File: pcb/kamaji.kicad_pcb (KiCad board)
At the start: 2 copper layers, 130 x 110 mm, 35 parts, among them J1 RJ10, J2 RJ10, J3 RJ10, J4 RJ10, J5 RJ10, Q1 TIP120, Q2 TIP120, SW1 CTRL1, SW2 CTRL2, SW3 CTRL3, U1 ATMEGA328P-PU

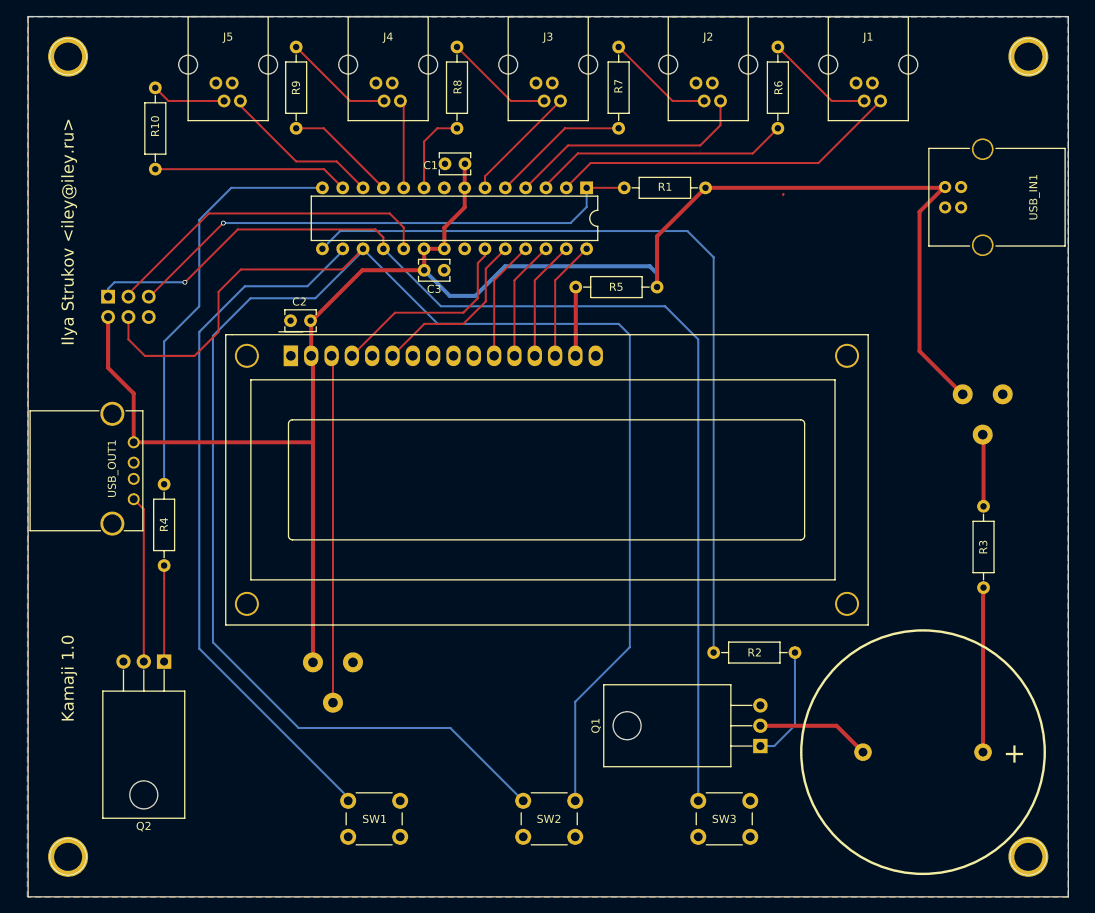
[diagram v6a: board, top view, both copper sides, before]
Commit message: replace TIP120 with a MOSFET, drive the speaker directly
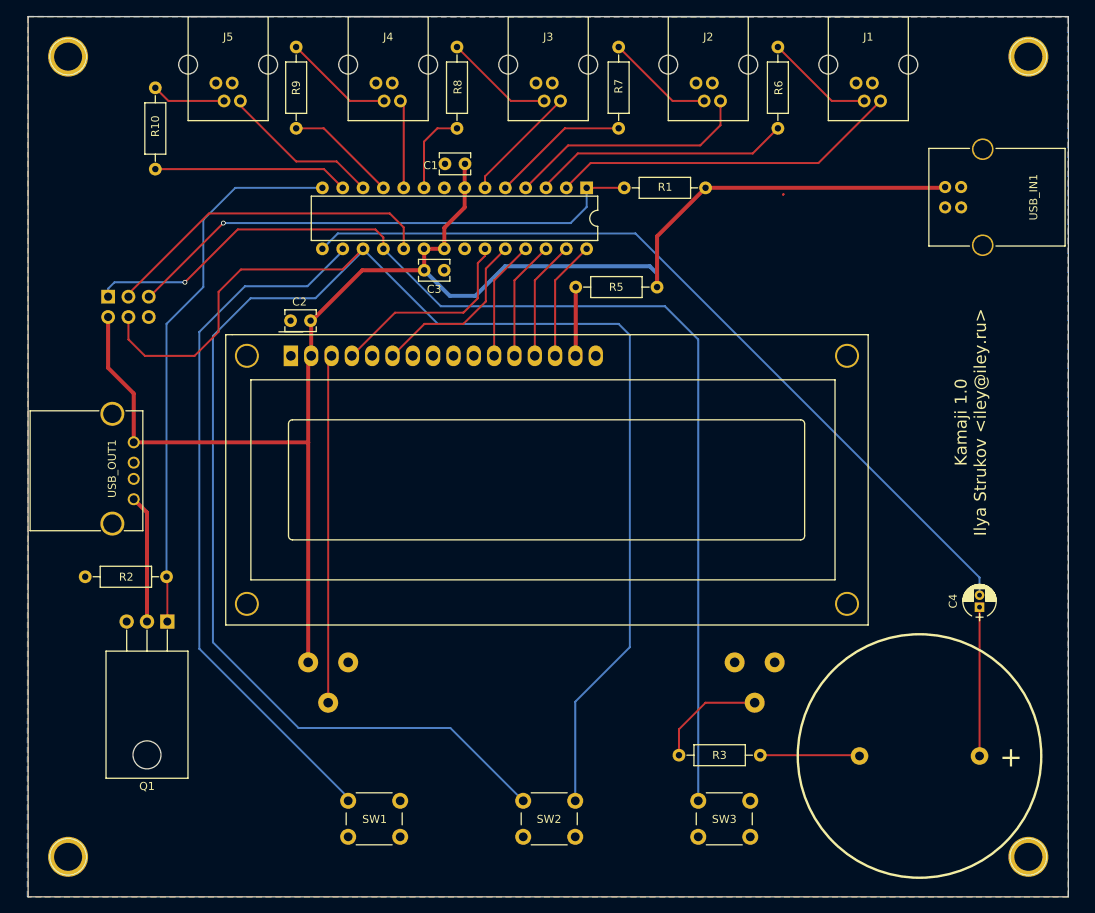
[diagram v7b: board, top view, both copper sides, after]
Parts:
- removed Q2: TIP120, TO_SOT_Packages_THT:TO-220_Horizontal
- removed R4: 2.2K, Resistors_THT:R_Axial_DIN0207_L6.3mm_D2.5mm_P10.16mm_Horizontal
- added C4: 47u, Capacitors_THT:CP_Radial_D4.0mm_P1.50mm, F.Cu at (218.9, 103.8)
- Q1: value TIP120 -> IRF540N
- R2: value 220R -> 10K
- R3: value 20R -> 100R
- moved R2 79.1 mm to (117.3, 100.0)
- moved Q1 75.7 mm to (117.4, 105.6), turned to 180 degrees
- moved RV1 44.0 mm to (188.3, 110.7)
- moved R3 41.8 mm to (191.5, 122.3), turned to 180 degrees
- moved LS1 0.65 mm to (211.4, 122.4)
- moved RV2 0.60 mm to (135.0, 110.7)
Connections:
- DS1 pad 10: Net-(DS1-Pad10) -> (no net)
- DS1 pad 7: Net-(DS1-Pad7) -> (no net)
- DS1 pad 8: Net-(DS1-Pad8) -> (no net)
- DS1 pad 9: Net-(DS1-Pad9) -> (no net)
- LS1 pad 1: Net-(LS1-Pad1) -> Net-(C4-Pad1)
- Q1 pad 1: Net-(Q1-Pad1) -> LAMP
- Q1 pad 2: Net-(LS1-Pad2) -> Net-(Q1-Pad2)
- R2 pad 1: Net-(Q1-Pad1) -> LAMP
- R2 pad 2: SND -> GND
- R3 pad 1: Net-(R3-Pad1) -> Net-(LS1-Pad2)
- R3 pad 2: Net-(LS1-Pad1) -> Net-(R3-Pad2)
- RV1 pad 1: VCC -> (no net)
- RV1 pad 2: Net-(R3-Pad1) -> Net-(R3-Pad2)
- RV1 pad 3: Net-(RV1-Pad3) -> GND
- USB_IN1 pad 2: Net-(USB_IN1-Pad2) -> (no net)
- USB_IN1 pad 3: Net-(USB_IN1-Pad3) -> (no net)
- USB_OUT1 pad 2: Net-(USB_OUT1-Pad2) -> (no net)
- USB_OUT1 pad 3: Net-(USB_OUT1-Pad3) -> (no net)
- USB_OUT1 pad 4: Net-(Q2-Pad2) -> Net-(Q1-Pad2)
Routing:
- net VCC: track 224.5 -> 195.0 mm
- net Net-(Q2-Pad2): track 20.8 -> 0.00 mm
- net Net-(LS1-Pad1): track 20.6 -> 0.00 mm
- net Net-(C4-Pad1): track 0.00 -> 18.6 mm
- net LAMP: track 51.9 -> 68.7 mm
- net Net-(Q1-Pad2): track 0.00 -> 16.0 mm
- net Net-(Q1-Pad1): track 14.5 -> 0.00 mm
- net Net-(R3-Pad2): track 0.00 -> 14.1 mm
- net Net-(Q2-Pad1): track 12.0 -> 0.00 mm
- net Net-(R3-Pad1): track 9.14 -> 0.00 mm
- net SND: track 100.6 -> 102.9 mm
- net Net-(LS1-Pad2): track 14.2 -> 12.6 mm
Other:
- board text added: "Kamaji 1.0 Ilya Strukov <iley@iley.ru>"
- board text removed: "Ilya Strukov <iley@iley.ru>"
- board text removed: "Kamaji 1.0"

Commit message: fix mounting holes
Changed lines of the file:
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@@
     (mod_text_width 0.15)
     (pad_size 5 5)
-    (pad_drill 3.5)
+    (pad_drill 3.3)
     (pad_to_mask_clearance 0.2)
     (aux_axis_origin 100 30)
@@
     (add_net "Net-(Q1-Pad2)")
     (add_net VCC)
+  )
+  (module Connectors:1pin (layer F.Cu)
+    (at 225 35)
+    (descr "module 1 pin (ou trou mecanique de percage)")
+    (tags DEV)
+    (fp_text reference REF** (at 0 -3.048) (layer F.SilkS) hide
+      (effects (font (size 1 1) (thickness 0.15)))
+    )
+    (fp_text value 1pin (at 0 3) (layer F.Fab) hide
+      (effects (font (size 1 1) (thickness 0.15)))
+    )
+    (fp_circle (center 0 0) (end 2 0.8) (layer F.Fab) (width 0.1))
+    (fp_circle (center 0 0) (end 2.6 0) (layer F.CrtYd) (width 0.05))
+    (fp_circle (center 0 0) (end 0 -2.286) (layer F.SilkS) (width 0.12))
+    (pad 1 thru_hole circle (at 0 0) (size 5 5) (drill 3.3) (layers *.Cu *.Mask))
+  )
+  (module Connectors:1pin (layer F.Cu)
+    (at 225 135)
+    (descr "module 1 pin (ou trou mecanique de percage)")
+    (tags DEV)
+    (fp_text reference REF** (at 0 -3.048) (layer F.SilkS) hide
+      (effects (font (size 1 1) (thickness 0.15)))
+    )
+    (fp_text value 1pin (at 0 3) (layer F.Fab) hide
+      (effects (font (size 1 1) (thickness 0.15)))
+    )
+    (fp_circle (center 0 0) (end 2 0.8) (layer F.Fab) (width 0.1))
+    (fp_circle (center 0 0) (end 2.6 0) (layer F.CrtYd) (width 0.05))
+    (fp_circle (center 0 0) (end 0 -2.286) (layer F.SilkS) (width 0.12))
+    (pad 1 thru_hole circle (at 0 0) (size 5 5) (drill 3.3) (layers *.Cu *.Mask))
+  )
+  (module Connectors:1pin (layer F.Cu)
+    (at 105 135)
+    (descr "module 1 pin (ou trou mecanique de percage)")
+    (tags DEV)
+    (fp_text reference REF** (at 0 -3.048) (layer F.SilkS) hide
+      (effects (font (size 1 1) (thickness 0.15)))
+    )
+    (fp_text value 1pin (at 0 3) (layer F.Fab) hide
+      (effects (font (size 1 1) (thickness 0.15)))
+    )
+    (fp_circle (center 0 0) (end 2 0.8) (layer F.Fab) (width 0.1))
+    (fp_circle (center 0 0) (end 2.6 0) (layer F.CrtYd) (width 0.05))
+    (fp_circle (center 0 0) (end 0 -2.286) (layer F.SilkS) (width 0.12))
+    (pad 1 thru_hole circle (at 0 0) (size 5 5) (drill 3.3) (layers *.Cu *.Mask))
   )
   (module Capacitors_THT:C_Disc_D3.8mm_W2.6mm_P2.50mm (layer F.Cu)
@@
     (fp_circle (center 0 0) (end 2.6 0) (layer F.CrtYd) (width 0.05))
     (fp_circle (center 0 0) (end 0 -2.286) (layer F.SilkS) (width 0.12))
-    (pad 1 thru_hole circle (at 0 0) (size 5 5) (drill 3.5) (layers *.Cu *.Mask))
-  )
-  (module Connectors:1pin (layer F.Cu)
-    (at 105 135)
-    (descr "module 1 pin (ou trou mecanique de percage)")
-    (tags DEV)
-    (fp_text reference REF** (at 0 -3.048) (layer F.SilkS) hide
-      (effects (font (size 1 1) (thickness 0.15)))
-    )
-    (fp_text value 1pin (at 0 3) (layer F.Fab) hide
-      (effects (font (size 1 1) (thickness 0.15)))
-    )
-    (fp_circle (center 0 0) (end 2 0.8) (layer F.Fab) (width 0.1))
-    (fp_circle (center 0 0) (end 2.6 0) (layer F.CrtYd) (width 0.05))
-    (fp_circle (center 0 0) (end 0 -2.286) (layer F.SilkS) (width 0.12))
-    (pad 1 thru_hole circle (at 0 0) (size 5 5) (drill 3.5) (layers *.Cu *.Mask))
-  )
-  (module Connectors:1pin (layer F.Cu)
-    (at 225 135)
-    (descr "module 1 pin (ou trou mecanique de percage)")
-    (tags DEV)
-    (fp_text reference REF** (at 0 -3.048) (layer F.SilkS) hide
-      (effects (font (size 1 1) (thickness 0.15)))
-    )
-    (fp_text value 1pin (at 0 3) (layer F.Fab) hide
-      (effects (font (size 1 1) (thickness 0.15)))
-    )
-    (fp_circle (center 0 0) (end 2 0.8) (layer F.Fab) (width 0.1))
-    (fp_circle (center 0 0) (end 2.6 0) (layer F.CrtYd) (width 0.05))
-    (fp_circle (center 0 0) (end 0 -2.286) (layer F.SilkS) (width 0.12))
-    (pad 1 thru_hole circle (at 0 0) (size 5 5) (drill 3.5) (layers *.Cu *.Mask))
-  )
-  (module Connectors:1pin (layer F.Cu)
-    (at 225 35)
-    (descr "module 1 pin (ou trou mecanique de percage)")
-    (tags DEV)
-    (fp_text reference REF** (at 0 -3.048) (layer F.SilkS) hide
-      (effects (font (size 1 1) (thickness 0.15)))
-    )
-    (fp_text value 1pin (at 0 3) (layer F.Fab) hide
-      (effects (font (size 1 1) (thickness 0.15)))
-    )
-    (fp_circle (center 0 0) (end 2 0.8) (layer F.Fab) (width 0.1))
-    (fp_circle (center 0 0) (end 2.6 0) (layer F.CrtYd) (width 0.05))
-    (fp_circle (center 0 0) (end 0 -2.286) (layer F.SilkS) (width 0.12))
-    (pad 1 thru_hole circle (at 0 0) (size 5 5) (drill 3.5) (layers *.Cu *.Mask))
+    (pad 1 thru_hole circle (at 0 0) (size 5 5) (drill 3.3) (layers *.Cu *.Mask))
   )
   (gr_text VOLUME (at 190.8 119) (layer B.SilkS)
